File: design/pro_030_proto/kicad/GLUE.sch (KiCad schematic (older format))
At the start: 13 parts, among them IC13 74HCT174, X2 8MHz

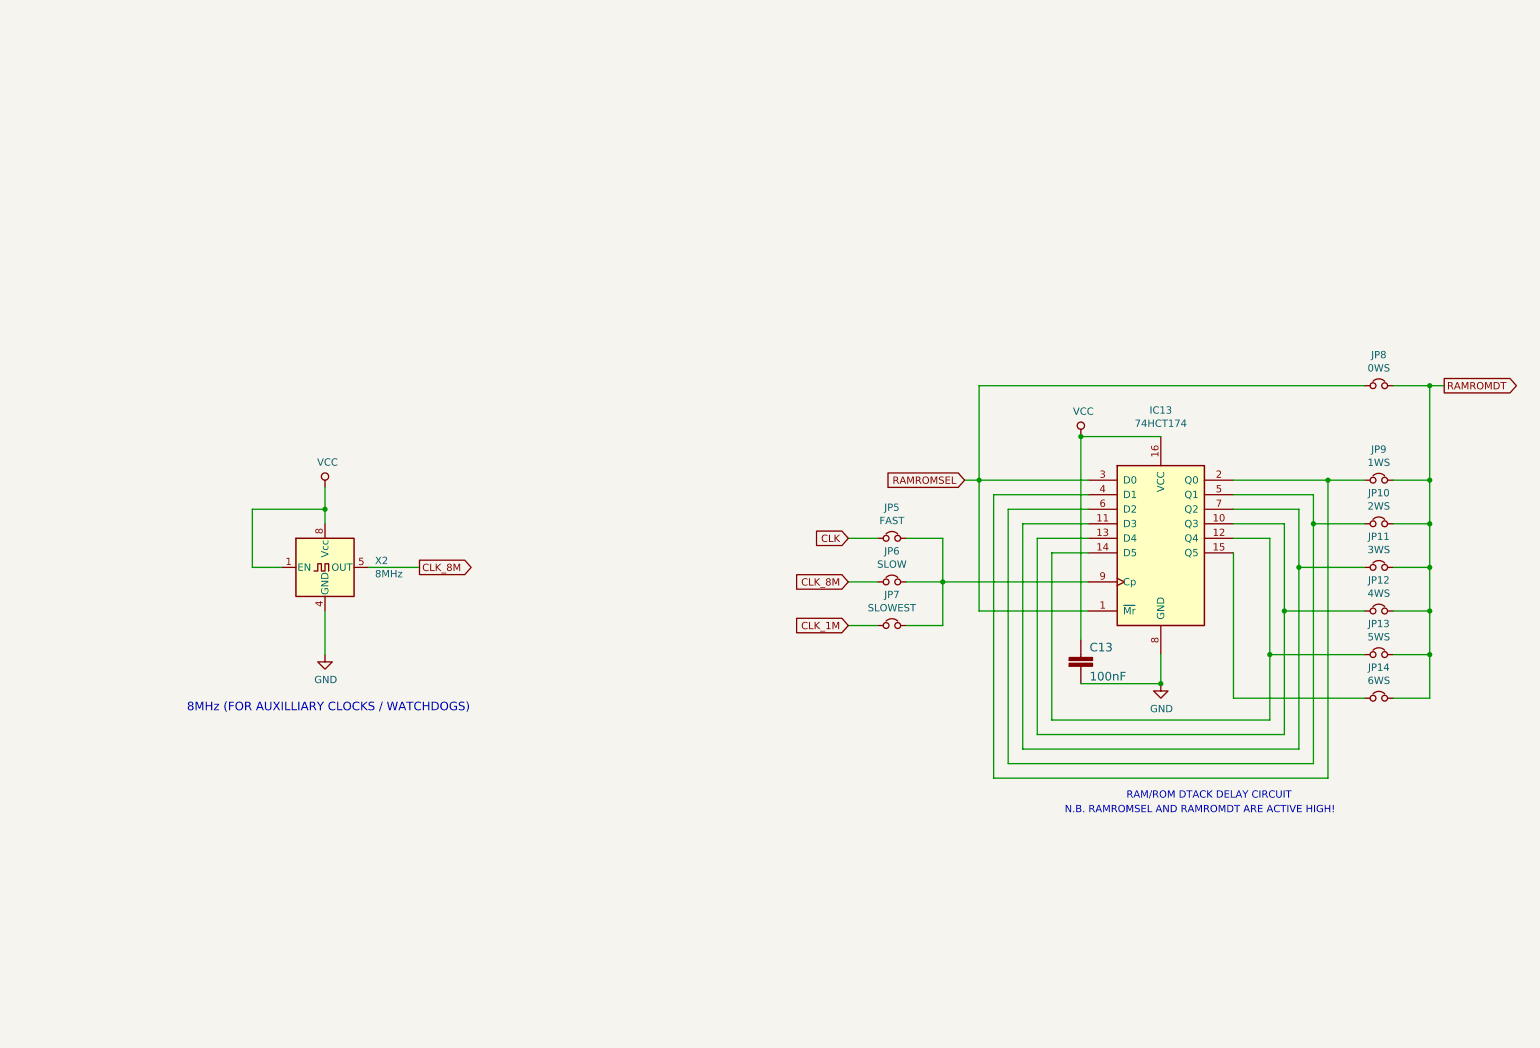
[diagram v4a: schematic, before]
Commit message: Lots more changes
* Add DIN expansion connectors (provisional pinout)
* Fix incorrect address lines for RAM & ROM (Doh!)
* Remove unused level shifters
* Fix clock enables
* Lots of other small fixes
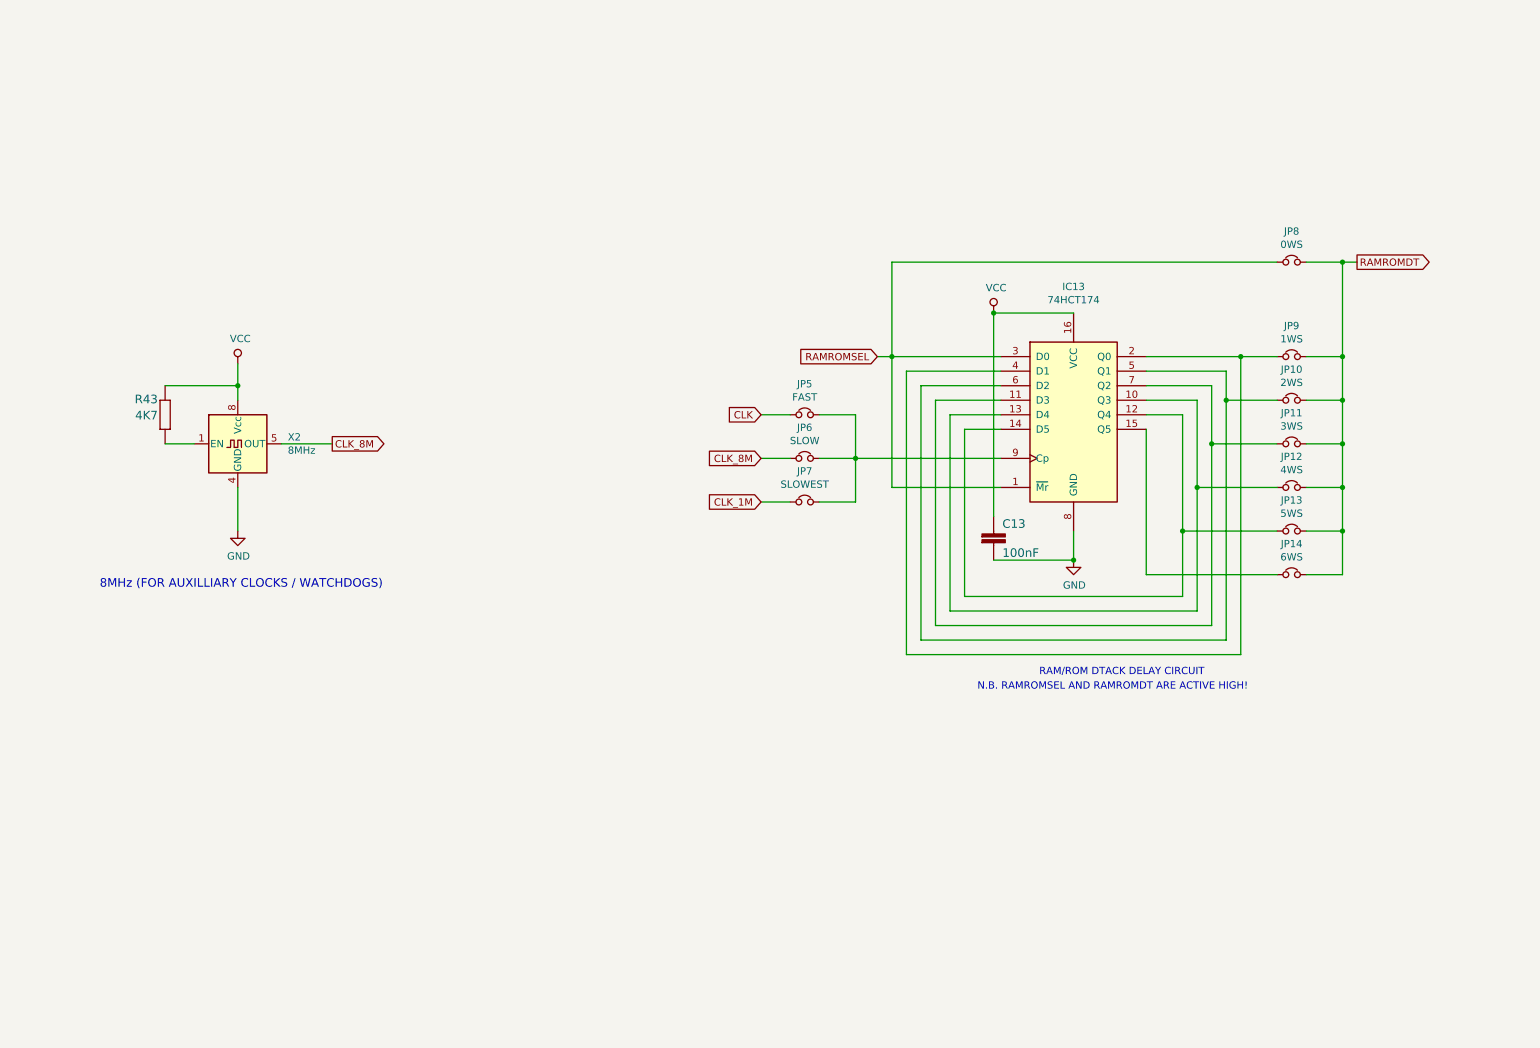
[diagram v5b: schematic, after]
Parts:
- added R43: 4K7, rosco_m68k:R-0207_10, symbol rosco_m68k-eagle-import:R-EU_0207_10
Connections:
- net VCC: now also R43.2; no longer X2.1 (EN)
- new net: R43.1, X2.1 (EN)
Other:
- moved on the sheet: C13, IC13, JP10, JP11, JP12, JP13, JP14, JP5, JP6, JP7, JP8, JP9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
